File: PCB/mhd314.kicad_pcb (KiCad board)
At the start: 4 copper layers, 65 x 56 mm, 189 parts, among them J1 Raspberry_Pi_2_3, J2 AudioJack_Pentaconn, J4 AudioJack3_SwitchTR, Q1 AO3401A, SW1 SW_Push, U1 ES9038Q2M, U10 AT24CS64-SSHM, U11 OPA1622, U13 OPA1622, U2 OPA1612AxD, U3 OPA1612AxD, U4 OPA1622, U5 LM317_SOT-223, U6 LM317_SOT-223, U7 TPS65131RGE, U8 LM317_SOT-223, U9 LM337_SOT223, Y1 ASE-50MHz

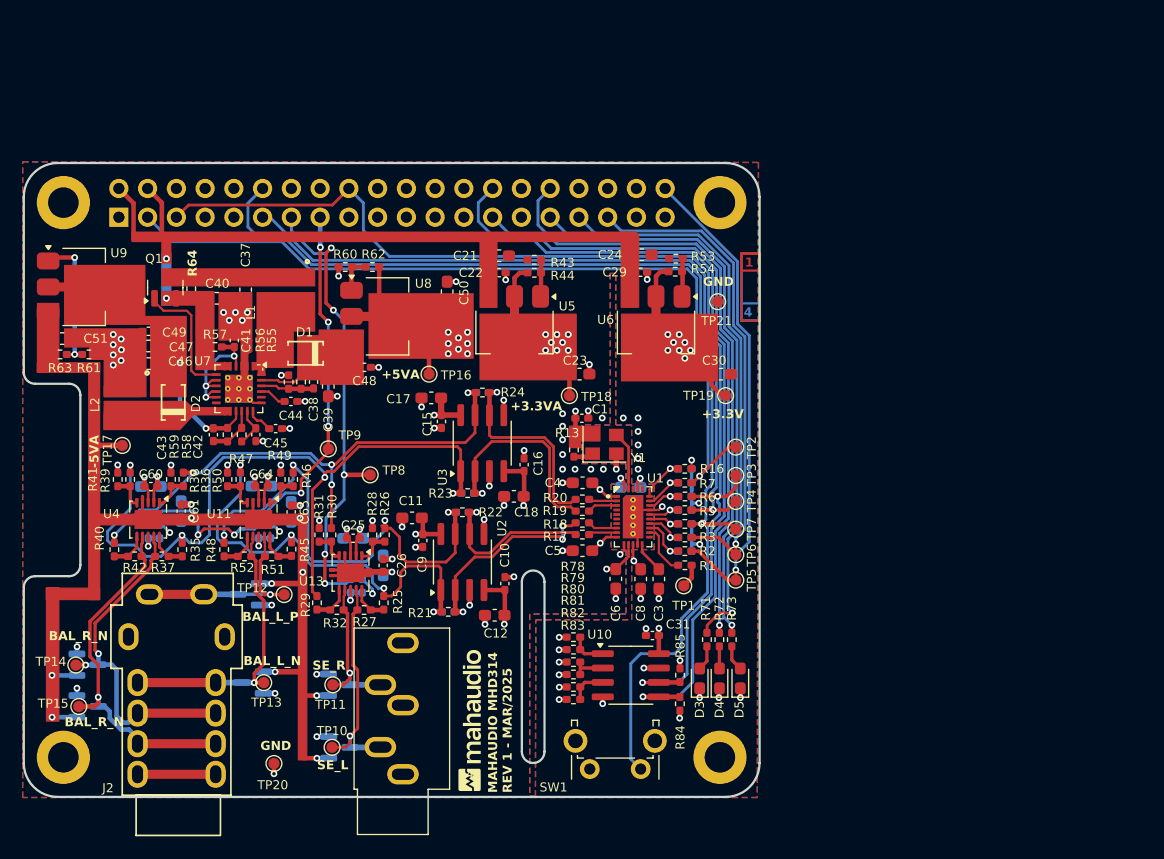
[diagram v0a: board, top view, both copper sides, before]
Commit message: Changed the 4.4mm connector and fixed a bunch o library related problems
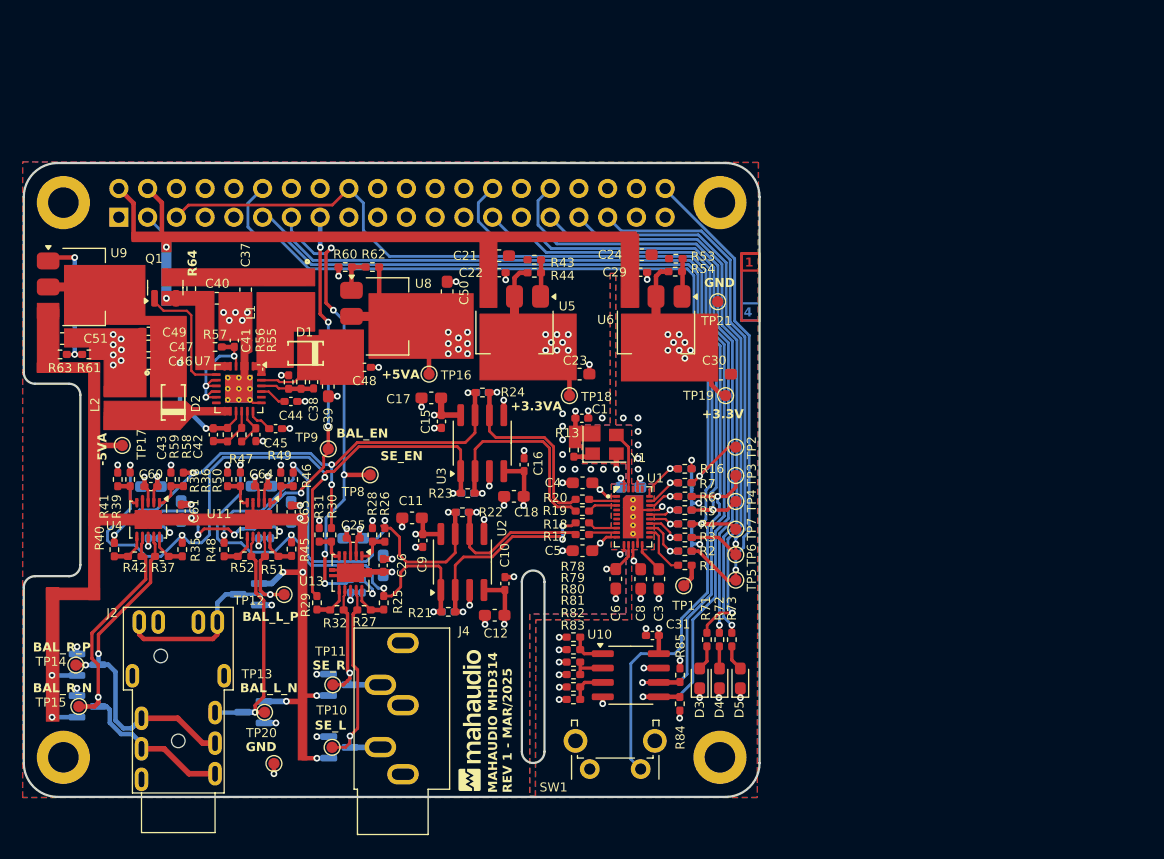
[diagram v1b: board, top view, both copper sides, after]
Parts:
- J2: footprint mahaudio KiCad Library:Jack_4.4mm_Pentaconn_NBA1-24-001_Horizontal -> mahaudio KiCad Library:Jack_4.4mm_G-Switch_GT-3321667P-01_Horizontal
- J4: footprint mahaudio KiCad Library:Jack_3.5mm_CUI_SJ1-3535NG_Horizontal_3D -> Connector_Audio:Jack_3.5mm_CUI_SJ1-3535NG_Horizontal
- moved J2 13.0 mm to (76.9, 110.7)
- moved D9 2.62 mm to (86.8, 104.8)
- moved TP13 2.62 mm to (87.8, 104.8)
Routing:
- net GND: track 79.2 -> 72.3 mm
- net /OUT_BAL_L_P: track 17.9 -> 23.3 mm
- net /OUT_BAL_L_N: track 25.2 -> 21.0 mm
- net /OUT_BAL_R_N: track 32.2 -> 34.4 mm
- net /OUT_BAL_R_P: track 31.4 -> 33.5 mm
- net /DAC_OUT_L_P: track 18.1 -> 18.7 mm
- net -5VA: track 40.6 -> 40.1 mm
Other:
- board text added: "BAL_EN"
- board text added: "BAL_R_P"
- board text added: "SE_EN"

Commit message: Increased trace width and clearance to 0.15mm. Changed the Pentaconn connector to JLCPCB supported part from GSwitch
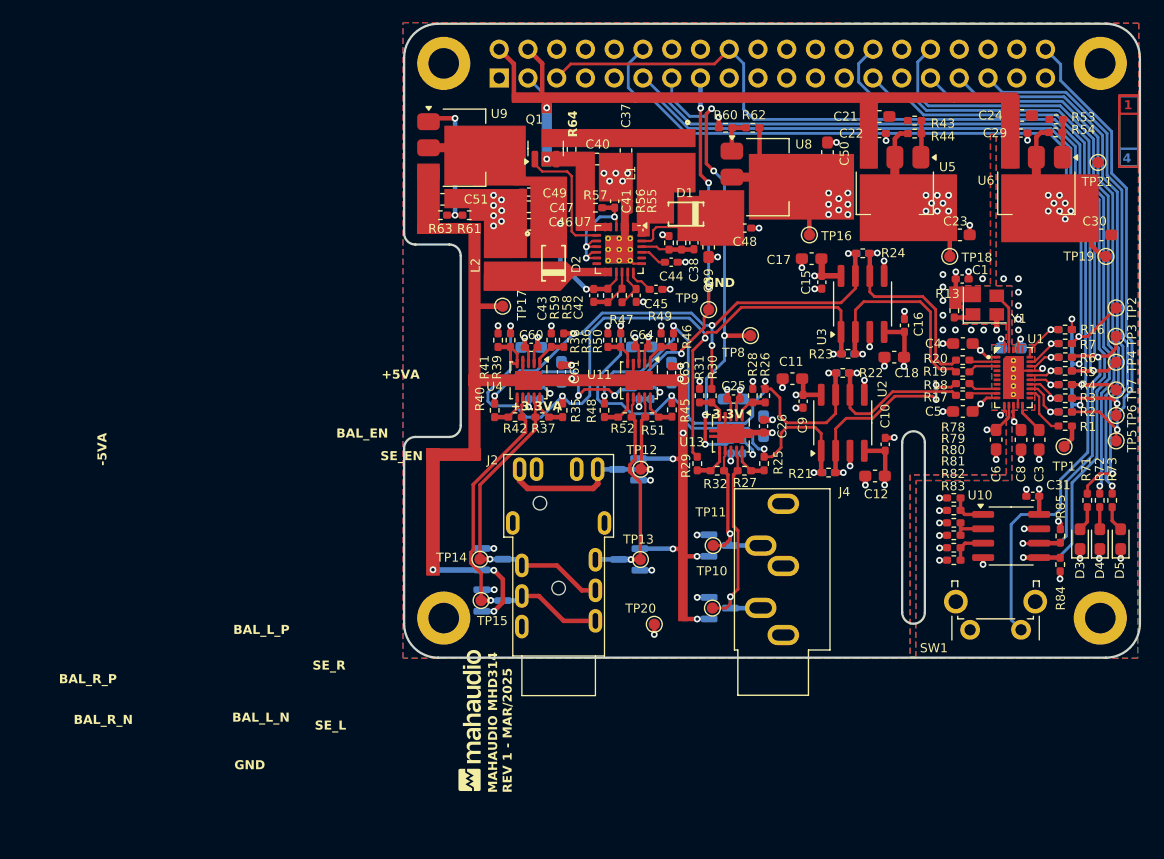
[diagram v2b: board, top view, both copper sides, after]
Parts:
- moved D11 37.0 mm to (107.9, 94.9)
- moved D10 37.0 mm to (107.9, 91.2)
- moved TP14 36.9 mm to (106.8, 91.2)
- moved TP15 36.7 mm to (106.9, 94.9)
- moved J2 36.2 mm to (110.5, 97.2)
- moved TP13 35.8 mm to (121.0, 91.3)
- moved D9 35.8 mm to (120.0, 91.3)
- moved C1 35.8 mm to (149.4, 66.5)
- moved C11 35.8 mm to (134.4, 75.3)
- moved C16 35.8 mm to (144.3, 70.6)
- moved C18 35.8 mm to (143.4, 73.4)
- moved C20 35.8 mm to (140.6, 64.2)
- moved C37 35.8 mm to (119.7, 55.1)
- moved C38 35.8 mm to (125.7, 63.3)
- moved C4 35.8 mm to (149.5, 72.2)
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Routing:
- net -5VA: track 40.1 -> 46.4 mm, vias 12 -> 13
- net /OUT_BAL_R_P: track 33.5 -> 27.7 mm, vias 2 -> 1
- net /BRD_ONOFF: track 110.7 -> 107.6 mm
- net /OUT_BAL_R_N: track 34.4 -> 31.7 mm
- net /OUT_BAL_L_N: track 21.0 -> 19.4 mm
- net /DAC_PCM_CLK: track 74.3 -> 72.7 mm
- net /DAC_SDA: track 74.2 -> 72.7 mm
- net /OUT_BAL_L_P: track 23.3 -> 21.8 mm
- net Net-(U4B-+): track 3.03 -> 4.47 mm
- net /DAC_RESETB: track 70.1 -> 68.7 mm
- net /DAC_PCM_FS: track 44.0 -> 43.0 mm
- net /BRD_ID_SC: track 70.8 -> 69.9 mm
- net /BRD_LED2: track 50.8 -> 49.9 mm
- net /BRD_ID_SD: track 68.1 -> 67.2 mm
- net /BRD_LED1: track 50.2 -> 49.3 mm
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
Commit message: Changed resistor values to match JLCPCB + general board revision
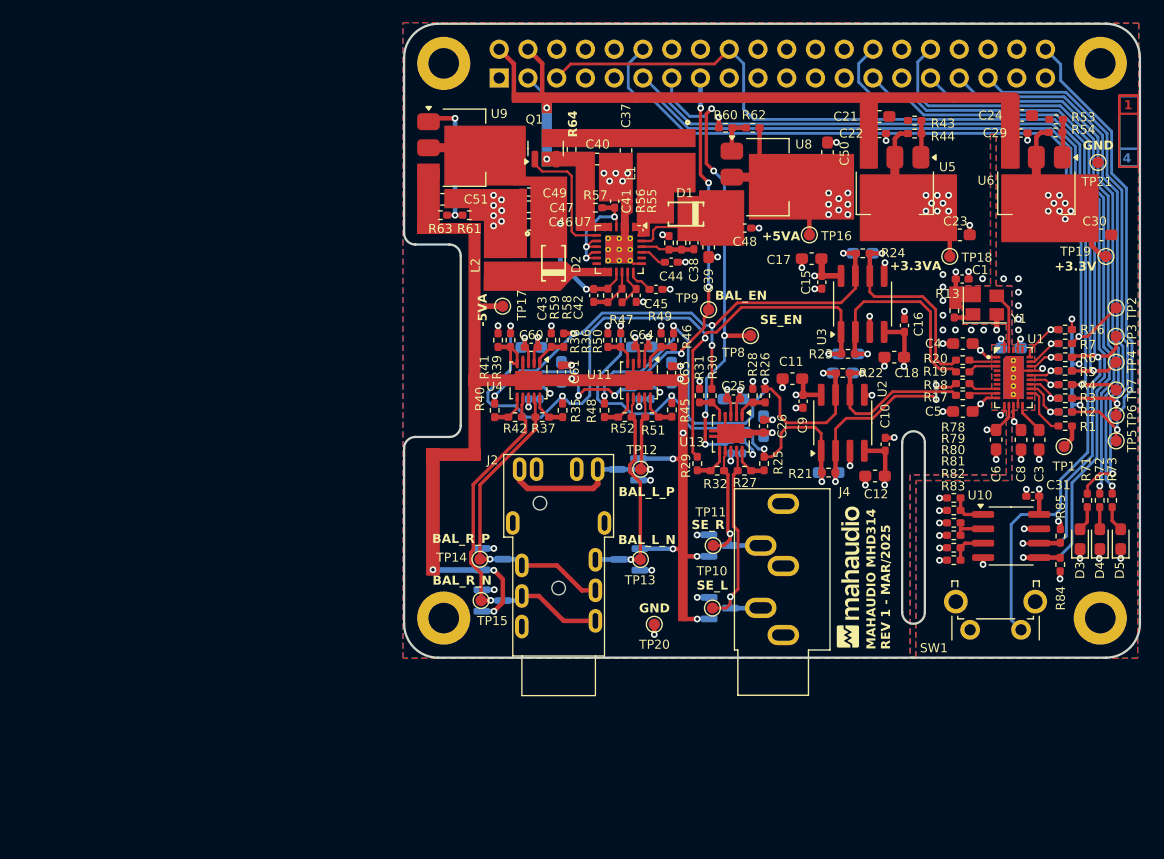
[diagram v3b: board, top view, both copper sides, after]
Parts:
- C13, C14, C19, C20: footprint Capacitor_SMD:C_0402_1005Metric_Pad0.74x0.62mm_HandSolder -> Capacitor_SMD:C_0603_1608Metric_Pad1.08x0.95mm_HandSolder
- moved G*** 35.7 mm to (139.3, 92.8)
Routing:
- net GND: track 72.8 -> 72.1 mm
- net /AMP/BalDiffAmp_L/BALDIFFAMP_IN_N: track 44.6 -> 45.2 mm
- net /DAC_OUT_L_N: track 15.0 -> 15.5 mm
- net /DAC_OUT_R_P: track 19.6 -> 20.1 mm
- net /AMP/BalDiffAmp_R/BALDIFFAMP_IN_P: track 66.8 -> 67.4 mm

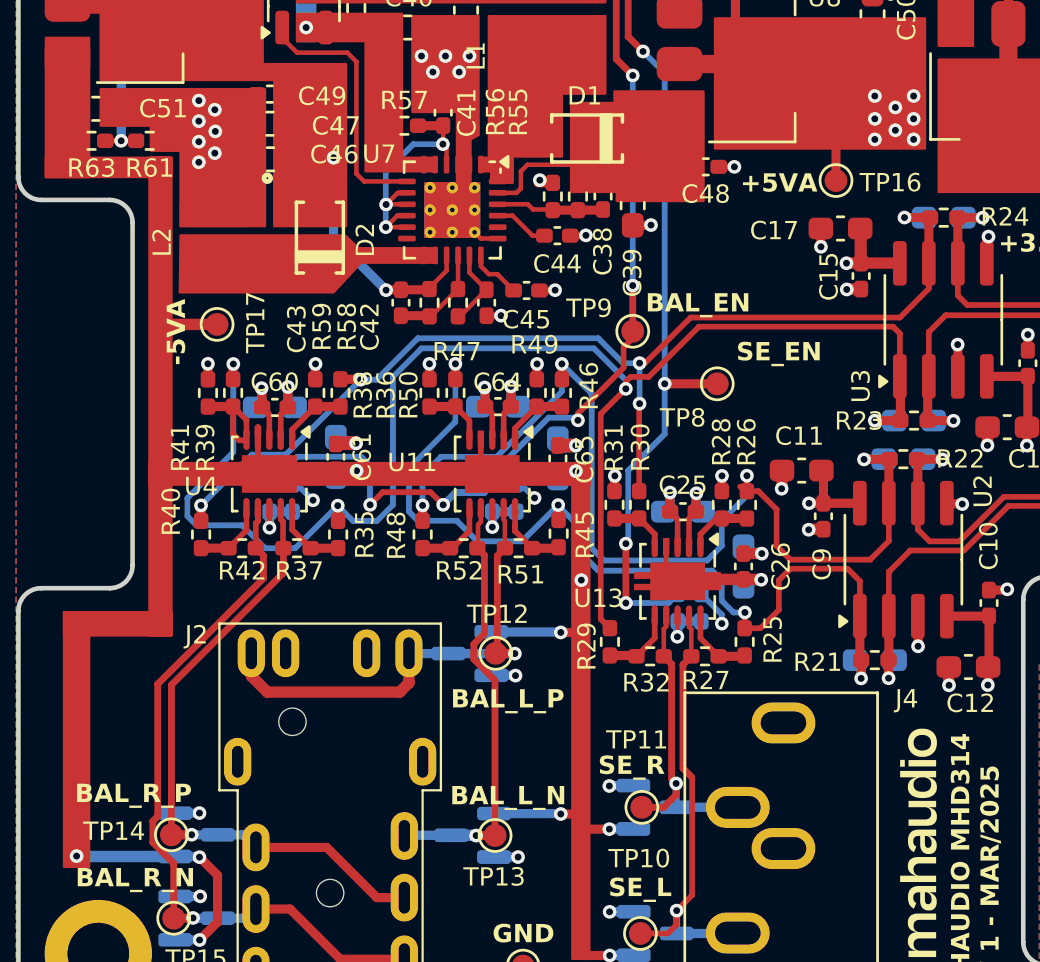
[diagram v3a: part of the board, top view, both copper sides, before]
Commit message: Added filter capacitors to OPA1622 circuitry
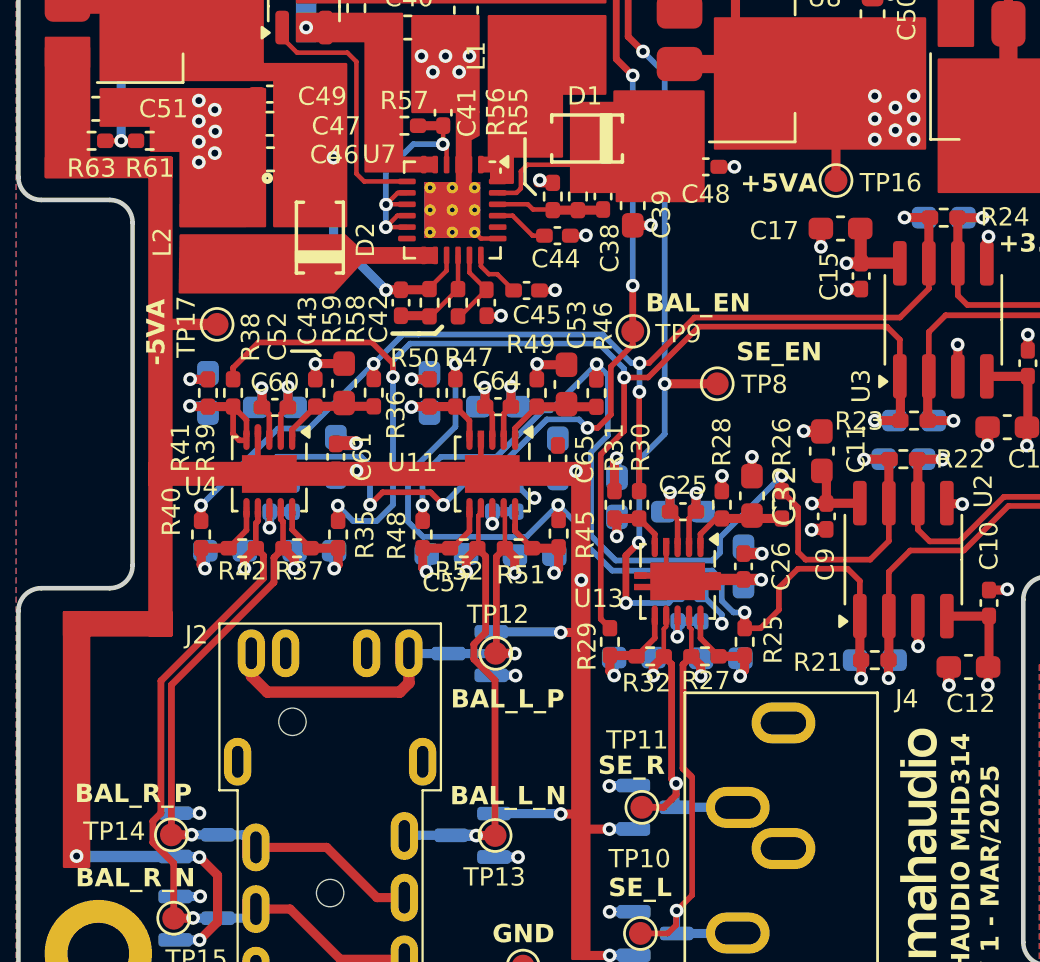
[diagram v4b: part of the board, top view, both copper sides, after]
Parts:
- added C2: DNP, Capacitor_SMD:C_0603_1608Metric_Pad1.08x0.95mm_HandSolder, B.Cu at (130.9, 83.5)
- added C32: DNP, Capacitor_SMD:C_0603_1608Metric_Pad1.08x0.95mm_HandSolder, F.Cu at (132.2, 76.4)
- added C33: DNP, Capacitor_SMD:C_0603_1608Metric_Pad1.08x0.95mm_HandSolder, B.Cu at (126.3, 76.5)
- added C34: DNP, Capacitor_SMD:C_0603_1608Metric_Pad1.08x0.95mm_HandSolder, B.Cu at (127.0, 83.5)
- added C35: DNP, Capacitor_SMD:C_0603_1608Metric_Pad1.08x0.95mm_HandSolder, B.Cu at (113.1, 78.8)
- added C36: DNP, Capacitor_SMD:C_0603_1608Metric_Pad1.08x0.95mm_HandSolder, B.Cu at (122.7, 79.0)
- added C52: DNP, Capacitor_SMD:C_0603_1608Metric_Pad1.08x0.95mm_HandSolder, F.Cu at (114.4, 71.5)
- added C53: DNP, Capacitor_SMD:C_0603_1608Metric_Pad1.08x0.95mm_HandSolder, F.Cu at (124.1, 71.5)
- added C54: DNP, Capacitor_SMD:C_0603_1608Metric_Pad1.08x0.95mm_HandSolder, B.Cu at (108.4, 71.9)
- added C55: DNP, Capacitor_SMD:C_0603_1608Metric_Pad1.08x0.95mm_HandSolder, B.Cu at (118.1, 71.9)
- added C56: DNP, Capacitor_SMD:C_0603_1608Metric_Pad1.08x0.95mm_HandSolder, B.Cu at (109.2, 78.8)
- added C57: DNP, Capacitor_SMD:C_0603_1608Metric_Pad1.08x0.95mm_HandSolder, B.Cu at (118.8, 79.0)
- R25, R26, R29, R30, R35, R36, R39, R40, R45, R46, R47, R48: value 481R -> 470R
- R27, R28, R31, R32: value 336R -> 330R
- moved R26 1.53 mm to (133.5, 76.8)
- moved R46 1.51 mm to (125.4, 71.9)
- moved R36 1.46 mm to (115.7, 71.9)
- moved C11 1.22 mm to (135.3, 74.5), turned to 90 degrees
- moved C9 0.13 mm to (135.5, 77.3)
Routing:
- net /AMP/BalDiffAmp_R/BALDIFFAMP_IN_P: track 67.4 -> 60.5 mm
- net GND: track 72.1 -> 76.2 mm, vias 87 -> 86
- net /OUT_BAL_L_N: track 19.4 -> 21.4 mm, vias 1 -> 2
- net /OUT_BAL_L_P: track 21.8 -> 23.8 mm, vias 1 -> 2
- net Net-(U11A--): track 4.29 -> 6.28 mm, vias 0 -> 1
- net Net-(U11B--): track 3.57 -> 5.45 mm, vias 0 -> 1
- net /OUT_BAL_R_N: track 31.7 -> 33.6 mm, vias 1 -> 2
- net /OUT_BAL_R_P: track 27.7 -> 29.6 mm, vias 1 -> 2
- net /OUT_SE_L: track 19.6 -> 21.4 mm, vias 1 -> 2
- net /OUT_SE_R: track 13.6 -> 15.4 mm, vias 1 -> 2
- net Net-(U13A--): track 3.29 -> 5.06 mm, vias 0 -> 1
- net Net-(U4B--): track 3.43 -> 5.18 mm, vias 0 -> 1
- net Net-(U4A--): track 3.66 -> 5.41 mm, vias 0 -> 1
- net /AMP_DIFF_EN: track 43.8 -> 45.5 mm
- net Net-(U13B--): track 4.33 -> 6.07 mm, vias 0 -> 1
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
